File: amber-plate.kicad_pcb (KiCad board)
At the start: 2 copper layers, 118.8 x 112.3 mm, 7 parts

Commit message: Remove the reset button cutout in the plate
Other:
- outline, holes or cut-outs redrawn
- board text added: "Amber plate v2"
- board text removed: "Amber plate v1"
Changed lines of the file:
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@@
   (general
     (thickness 1.6)
-    (drawings 225)
+    (drawings 222)
     (tracks 0)
     (zones 0)
@@
       (effects (font (size 1 1) (thickness 0.15)))
     )
+    (fp_circle (center 0 0) (end 5.3 0) (layer Cmts.User) (width 0.15))
     (fp_circle (center 0 0) (end 5.55 0) (layer F.CrtYd) (width 0.05))
-    (fp_circle (center 0 0) (end 5.3 0) (layer Cmts.User) (width 0.15))
     (fp_text user %R (at 0.3 0) (layer F.Fab)
       (effects (font (size 1 1) (thickness 0.15)))
@@
       (effects (font (size 1 1) (thickness 0.15)))
     )
+    (fp_circle (center 0 0) (end 5.3 0) (layer Cmts.User) (width 0.15))
     (fp_circle (center 0 0) (end 5.55 0) (layer F.CrtYd) (width 0.05))
-    (fp_circle (center 0 0) (end 5.3 0) (layer Cmts.User) (width 0.15))
     (fp_text user %R (at 0.3 0) (layer F.Fab)
       (effects (font (size 1 1) (thickness 0.15)))
@@
     (pad "" thru_hole circle (at 0 0) (size 4.2 4.2) (drill 2.3) (layers *.Cu *.Mask))
   )
-  (gr_text "Amber plate v1" (at 38.75 -22.75) (layer F.SilkS)
+  (gr_text "Amber plate v2" (at 38.75 -22.75) (layer F.SilkS)
     (effects (font (size 1 1) (thickness 0.15)))
   )
@@
     (effects (font (size 1 1) (thickness 0.15)))
   )
-  (gr_line (start 105.81798 30.4) (end 105.81798 0.5) (layer Edge.Cuts) (width 0.2))
-  (gr_line (start 101.5 -9.5) (end 105.81798 -9.5) (layer Edge.Cuts) (width 0.05))
-  (gr_line (start 101.5 0.5) (end 101.5 -9.5) (layer Edge.Cuts) (width 0.05))
-  (gr_line (start 105.81798 0.5) (end 101.5 0.5) (layer Edge.Cuts) (width 0.05))
+  (gr_line (start 105.81798 30.4) (end 105.81798 -9.5) (layer Edge.Cuts) (width 0.2))
   (gr_line (start 86.127343 26.915419) (end 81.09278 33.132587) (layer Edge.Cuts) (width 0.2))
   (gr_line (start 91.972823 41.943072) (end 97.007386 35.725905) (layer Edge.Cuts) (width 0.2))

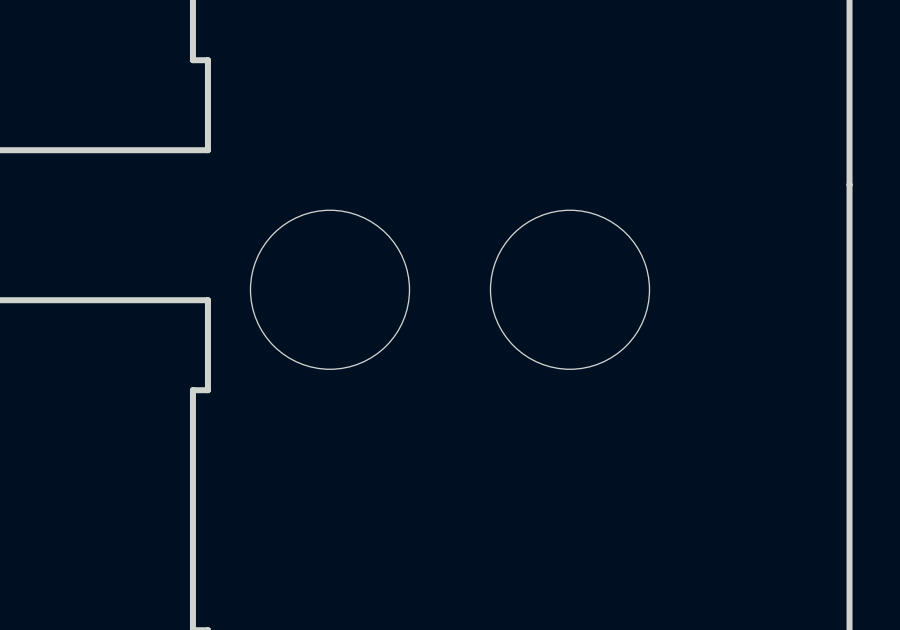
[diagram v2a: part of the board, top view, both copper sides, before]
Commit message: Replace 2 LEDs with one 5mm
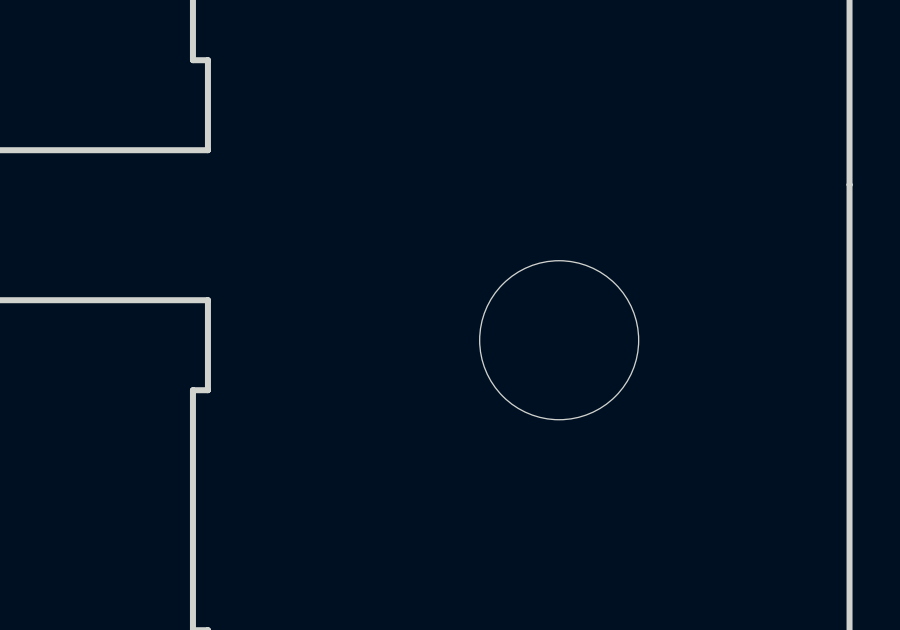
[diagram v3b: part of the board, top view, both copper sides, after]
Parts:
- removed D18, D19: LED, MountingHole:MountingHole_5.3mm_M5
- added REF**: MountingHole_5.3mm_M5, MountingHole:MountingHole_5.3mm_M5, F.Cu at (96.1, -4.32)
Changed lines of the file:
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@@
     (tracks 0)
     (zones 0)
-    (modules 7)
+    (modules 6)
     (nets 2)
   )
@@
   )
   (module MountingHole:MountingHole_5.3mm_M5 (layer F.Cu)
-    (at 88.5 -6)
+    (at 96.139 -4.318)
     (descr "Mounting Hole 5.3mm, no annular, M5")
     (tags "mounting hole 5.3mm no annular m5")
     (attr virtual)
-    (fp_text reference D18 (at 1.27 -2.96) (layer F.SilkS) hide
+    (fp_text reference REF** (at 0 -6.3) (layer F.SilkS) hide
       (effects (font (size 1 1) (thickness 0.15)))
     )
-    (fp_text value LED (at 1.27 2.96) (layer F.Fab)
+    (fp_text value MountingHole_5.3mm_M5 (at 0 6.3) (layer F.Fab)
       (effects (font (size 1 1) (thickness 0.15)))
     )
-    (fp_circle (center 0 0) (end 5.55 0) (layer F.CrtYd) (width 0.05))
-    (fp_circle (center 0 0) (end 5.3 0) (layer Cmts.User) (width 0.15))
     (fp_text user %R (at 0.3 0) (layer F.Fab)
       (effects (font (size 1 1) (thickness 0.15)))
     )
+    (fp_circle (center 0 0) (end 5.3 0) (layer Cmts.User) (width 0.15))
+    (fp_circle (center 0 0) (end 5.55 0) (layer F.CrtYd) (width 0.05))
     (pad 1 np_thru_hole circle (at 0 0) (size 5.3 5.3) (drill 5.3) (layers *.Cu *.Mask))
   )
-  (module MountingHole:MountingHole_5.3mm_M5 (layer F.Cu)
-    (at 96.5 -6)
-    (descr "Mounting Hole 5.3mm, no annular, M5")
-    (tags "mounting hole 5.3mm no annular m5")
-    (attr virtual)
-    (fp_text reference D19 (at 1.27 -2.96) (layer F.SilkS) hide
-      (effects (font (size 1 1) (thickness 0.15)))
-    )
-    (fp_text value LED (at 1.27 2.96) (layer F.Fab)
-      (effects (font (size 1 1) (thickness 0.15)))
-    )
-    (fp_circle (center 0 0) (end 5.55 0) (layer F.CrtYd) (width 0.05))
-    (fp_circle (center 0 0) (end 5.3 0) (layer Cmts.User) (width 0.15))
-    (fp_text user %R (at 0.3 0) (layer F.Fab)
-      (effects (font (size 1 1) (thickness 0.15)))
-    )
-    (pad 1 np_thru_hole circle (at 0 0) (size 5.3 5.3) (drill 5.3) (layers *.Cu *.Mask))
-  )
